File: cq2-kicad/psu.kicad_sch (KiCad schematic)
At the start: 0 parts

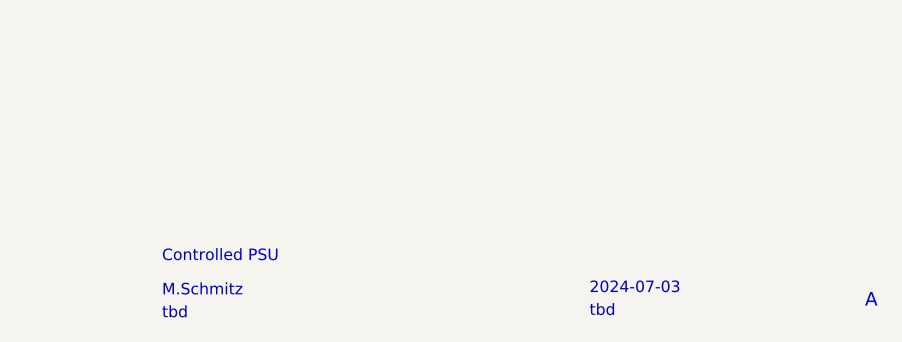
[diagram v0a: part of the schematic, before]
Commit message: drc checked before panalization
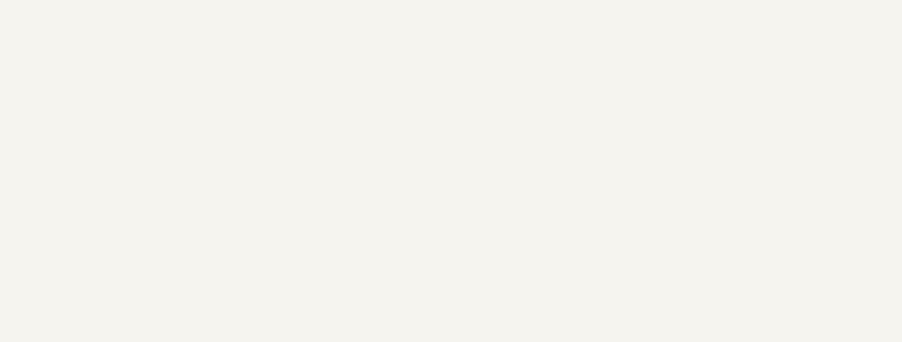
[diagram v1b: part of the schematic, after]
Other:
- note removed: "2024-07-03"
- note removed: "A"
- note removed: "Controlled PSU"
- note removed: "M.Schmitz"
- note removed: "tbd"
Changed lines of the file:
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@@
 	(title_block
 		(title "CQ2")
-		(date "2024-07-17")
+		(date "2024-07-31")
 		(rev "0")
+		(comment 1 "PSU Control")
+		(comment 2 "Manfred Schmitz")
+		(comment 3 "tbd")
+		(comment 4 "2024-07-03")
+		(comment 5 "tbd")
+		(comment 6 "A")
 	)
 	(wire
@@
 			(width 0)
 			(type default)
-		)
-	)
-	(text "M.Schmitz"
-		(exclude_from_sim no)
-		(at 190.246 191.262 0)
-		(effects
-			(font
-				(size 1.27 1.27)
-			)
-			(justify left bottom)
 		)
 	)
@@
 		)
 	)
-	(text "Controlled PSU"
-		(exclude_from_sim no)
-		(at 190.246 187.452 0)
-		(effects
-			(font
-				(size 1.27 1.27)
-			)
-			(justify left bottom)
-		)
-	)
 	(text "Functional Isolation"
 		(exclude_from_sim no)
@@
 			)
 			(justify left bottom)
-		)
-	)
-	(text "tbd"
-		(exclude_from_sim no)
-		(at 190.246 193.802 0)
-		(effects
-			(font
-				(size 1.27 1.27)
-			)
-			(justify left bottom)
-		)
-	)
-	(text "2024-07-03"
-		(exclude_from_sim no)
-		(at 237.744 191.008 0)
-		(effects
-			(font
-				(size 1.27 1.27)
-			)
-			(justify left bottom)
-		)
-	)
-	(text "tbd"
-		(exclude_from_sim no)
-		(at 237.744 193.548 0)
-		(effects
-			(font
-				(size 1.27 1.27)
-			)
-			(justify left bottom)
-		)
-	)
-	(text "A"
-		(exclude_from_sim no)
-		(at 268.351 192.532 0)
-		(effects
-			(font
-				(size 1.4986 1.4986)
-			)
-			(justify left bottom)
